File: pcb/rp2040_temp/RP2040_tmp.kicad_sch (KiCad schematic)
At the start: 34 parts, among them J2 Conn_01x04_Female

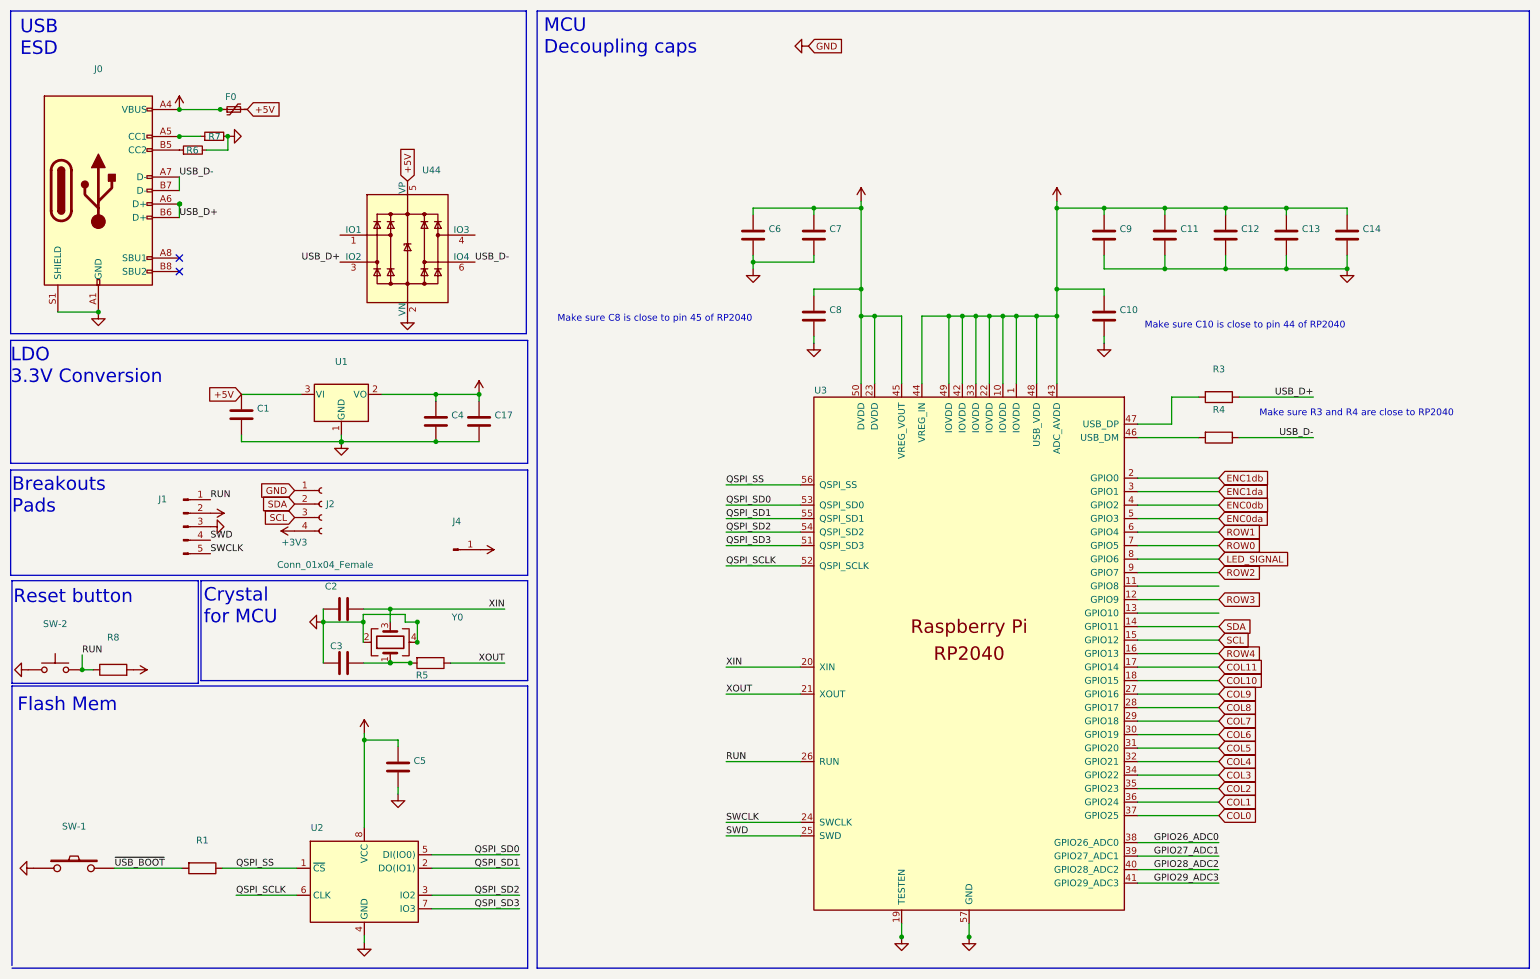
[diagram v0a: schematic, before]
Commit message: finalized placement and pcb
encoder and component placement was updated.
Further deleted backups from repo
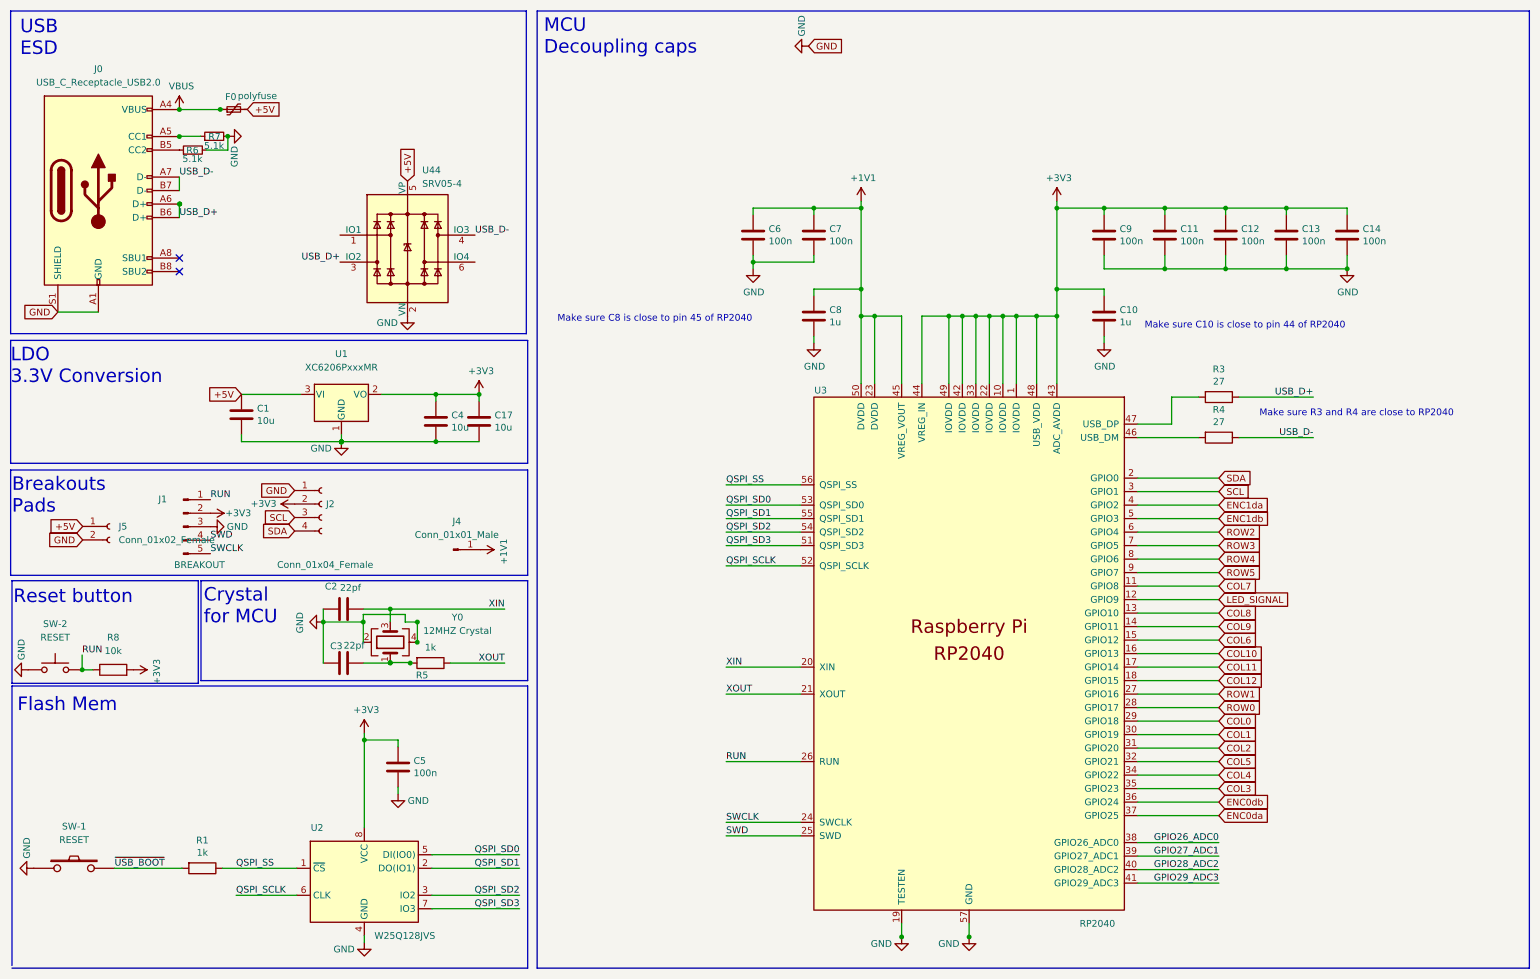
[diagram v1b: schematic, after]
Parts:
- removed U1: (no value), symbol Regulator_Linear:NCP1117-3.3_SOT223
- added J5: Conn_01x02_Female, Connector_PinHeader_2.54mm:PinHeader_1x02_P2.54mm_Vertical, symbol Connector:Conn_01x02_Female
- added U1: XC6206PxxxMR, Package_TO_SOT_SMD:SOT-23, symbol Regulator_Linear:XC6206PxxxMR
- C1, C17, C4: value (none) -> 10u; footprint (none) -> Capacitor_SMD:C_0805_2012Metric
- C10, C8: value (none) -> 1u; footprint (none) -> Capacitor_SMD:C_0805_2012Metric
- C11, C12, C13, C14, C5, C6, C7, C9: value (none) -> 100n; footprint (none) -> Capacitor_SMD:C_0805_2012Metric
- C2, C3: value (none) -> 22pf; footprint (none) -> Capacitor_SMD:C_0805_2012Metric
- F0: value (none) -> polyfuse; footprint (none) -> Fuse:Fuse_1206_3216Metric
- J0: value (none) -> USB_C_Receptacle_USB2.0; footprint (none) -> Connector_USB:USB_C_Receptacle_HRO_TYPE-C-31-M-12
- J1: value (none) -> BREAKOUT; footprint (none) -> Connector_PinSocket_2.54mm:PinSocket_1x05_P2.54mm_Vertical
- J2: footprint Connector_PinHeader_1.27mm:PinHeader_1x03_P1.27mm_Vertical -> Connector_PinHeader_2.54mm:PinHeader_1x04_P2.54mm_Vertical
- J4: value (none) -> Conn_01x01_Male; footprint (none) -> Connector_PinSocket_1.27mm:PinSocket_1x01_P1.27mm_Vertical
- R1, R5: value (none) -> 1k; footprint (none) -> Resistor_SMD:R_0805_2012Metric
- R3, R4: value (none) -> 27; footprint (none) -> Resistor_SMD:R_0805_2012Metric
- R6, R7: value (none) -> 5.1k; footprint (none) -> Resistor_SMD:R_0805_2012Metric
- R8: value (none) -> 10k; footprint (none) -> Resistor_SMD:R_0805_2012Metric
- SW-1, SW-2: value (none) -> RESET; footprint (none) -> Keebio-Parts:SW_SPST_TL3342
- U2: value (none) -> W25Q128JVS; footprint (none) -> Package_SO:SOIC-8_5.23x5.23mm_P1.27mm
- U3: value (none) -> RP2040; footprint (none) -> RP2040:RP2040-QFN-56
- U44: value (none) -> SRV05-4; footprint (none) -> Package_TO_SOT_SMD:SOT-23-6
- Y0: value (none) -> 12MHZ Crystal; footprint (none) -> Crystal:Crystal_SMD_3225-4Pin_3.2x2.5mm
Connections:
- net +3V3: now also J2.2 (Pin_2), U1.2 (VO); no longer J2.4 (Pin_4)
- net +5V: now also J5.1 (Pin_1), U1.3 (VI)
- net COL0: now also U3.29 (GPIO18); no longer U3.37 (GPIO25)
- net COL1: now also U3.30 (GPIO19); no longer U3.36 (GPIO24)
- net COL10: now also U3.16 (GPIO13); no longer U3.18 (GPIO15)
- net COL2: now also U3.31 (GPIO20); no longer U3.35 (GPIO23)
- net COL3: now also U3.35 (GPIO23); no longer U3.34 (GPIO22)
- net COL4: now also U3.34 (GPIO22); no longer U3.32 (GPIO21)
- net COL5: now also U3.32 (GPIO21); no longer U3.31 (GPIO20)
- net COL6: now also U3.15 (GPIO12); no longer U3.30 (GPIO19)
- net COL7: now also U3.11 (GPIO8); no longer U3.29 (GPIO18)
- net COL8: now also U3.13 (GPIO10); no longer U3.28 (GPIO17)
- net COL9: now also U3.14 (GPIO11); no longer U3.27 (GPIO16)
- net ENC0da: now also U3.37 (GPIO25); no longer U3.5 (GPIO3)
- net ENC0db: now also U3.36 (GPIO24); no longer U3.4 (GPIO2)
- net ENC1da: now also U3.4 (GPIO2); no longer U3.3 (GPIO1)
- net ENC1db: now also U3.5 (GPIO3); no longer U3.2 (GPIO0)
- net GND: now also J5.2 (Pin_2), U1.1 (GND)
- net LED_SIGNAL: now also U3.12 (GPIO9); no longer U3.8 (GPIO6)
- net ROW0: now also U3.28 (GPIO17); no longer U3.7 (GPIO5)
- net ROW1: now also U3.27 (GPIO16); no longer U3.6 (GPIO4)
- net ROW2: now also U3.6 (GPIO4); no longer U3.9 (GPIO7)
- net ROW3: now also U3.7 (GPIO5); no longer U3.12 (GPIO9)
- net ROW4: now also U3.8 (GPIO6); no longer U3.16 (GPIO13)
- net SCL: now also U3.3 (GPIO1); no longer U3.15 (GPIO12)
- net SDA: now also J2.4 (Pin_4), U3.2 (GPIO0); no longer J2.2 (Pin_2), U3.14 (GPIO11)
- net USB_D-: now also U44.4 (IO3); no longer U44.6 (IO4)
- new net COL12: U3.18 (GPIO15)
- new net ROW5: U3.9 (GPIO7)

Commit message: updated lcsc partnumber for ldo
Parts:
- U1: LCSC C3015484 -> C347376
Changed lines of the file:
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@@
       (effects (font (size 1.27 1.27)) hide)
     )
-    (property "LCSC" "C3015484" (id 4) (at 74.9431 176.53 0)
+    (property "LCSC" "C347376" (id 4) (at 74.9431 176.53 0)
       (effects (font (size 1.27 1.27)) hide)
     )
